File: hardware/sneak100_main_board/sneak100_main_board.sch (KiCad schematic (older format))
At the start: 0 parts

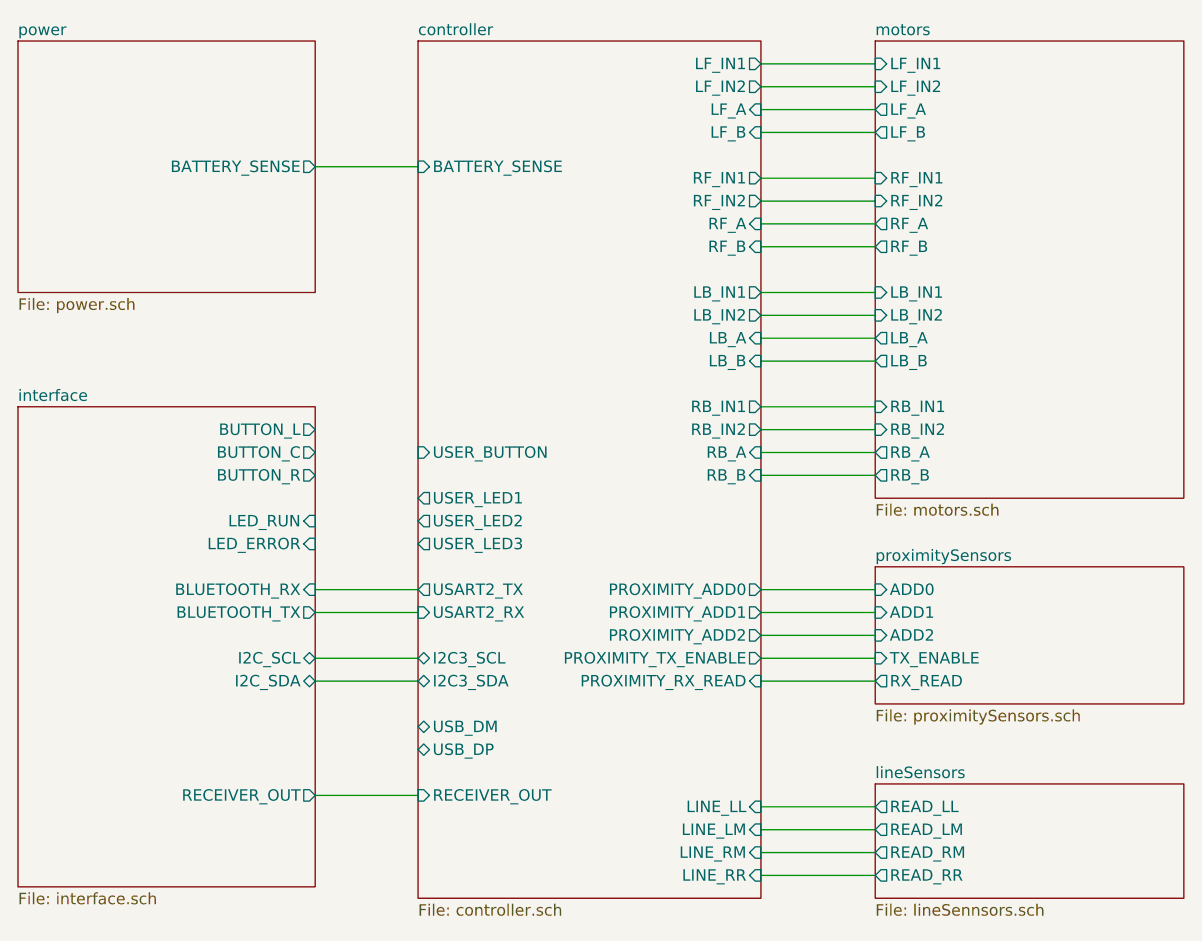
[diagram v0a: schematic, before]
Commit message: Board interface layout
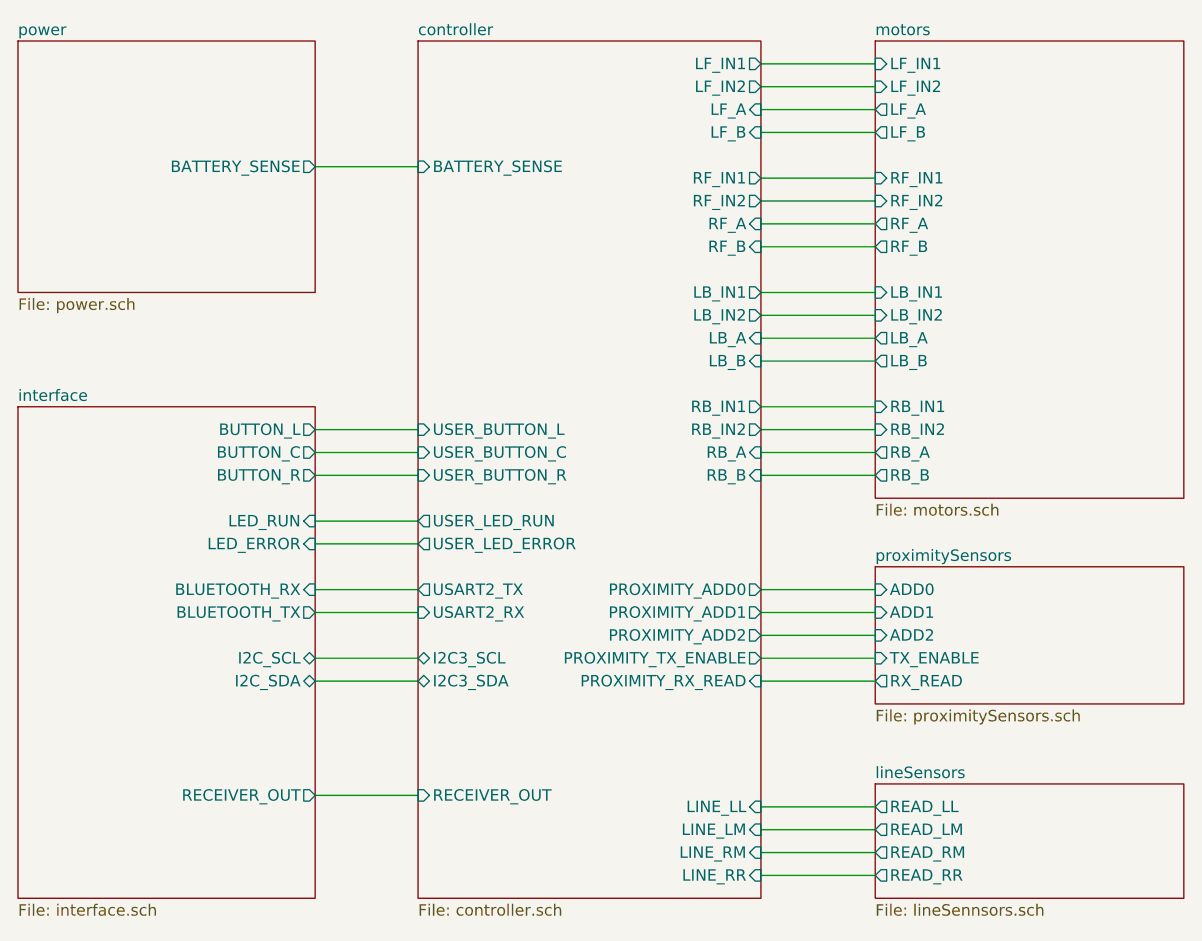
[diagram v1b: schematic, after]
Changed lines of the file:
@@
 F7 "LB_B" I R 6400 3300 50
 F8 "I2C3_SCL" B L 4900 4600 50
-F9 "USB_DM" B L 4900 4900 50
-F10 "USB_DP" B L 4900 5000 50
-F11 "USER_LED1" O L 4900 3900 50
-F12 "LB_IN1" O R 6400 3000 50
-F13 "LB_IN2" O R 6400 3100 50
-F14 "PROXIMITY_ADD0" O R 6400 4300 50
-F15 "PROXIMITY_ADD1" O R 6400 4400 50
-F16 "PROXIMITY_ADD2" O R 6400 4500 50
-F17 "RB_A" I R 6400 3700 50
-F18 "RB_B" I R 6400 3800 50
-F19 "RB_IN1" O R 6400 3500 50
-F20 "RB_IN2" O R 6400 3600 50
-F21 "RF_IN1" O R 6400 2500 50
-F22 "RF_IN2" O R 6400 2600 50
-F23 "LF_IN1" O R 6400 2000 50
-F24 "LF_IN2" O R 6400 2100 50
-F25 "LINE_LL" I R 6400 5250 50
-F26 "LINE_LM" I R 6400 5350 50
-F27 "LINE_RM" I R 6400 5450 50
-F28 "LINE_RR" I R 6400 5550 50
-F29 "BATTERY_SENSE" I L 4900 2450 50
-F30 "PROXIMITY_RX_READ" I R 6400 4700 50
-F31 "LF_A" I R 6400 2200 50
-F32 "LF_B" I R 6400 2300 50
-F33 "PROXIMITY_TX_ENABLE" O R 6400 4600 50
-F34 "I2C3_SDA" B L 4900 4700 50
-F35 "USER_LED2" O L 4900 4000 50
-F36 "USER_LED3" O L 4900 4100 50
-F37 "USER_BUTTON" I L 4900 3700 50
-F38 "RECEIVER_OUT" I L 4900 5200 50
+F9 "LB_IN1" O R 6400 3000 50
+F10 "LB_IN2" O R 6400 3100 50
+F11 "PROXIMITY_ADD0" O R 6400 4300 50
+F12 "PROXIMITY_ADD1" O R 6400 4400 50
+F13 "PROXIMITY_ADD2" O R 6400 4500 50
+F14 "RB_A" I R 6400 3700 50
+F15 "RB_B" I R 6400 3800 50
+F16 "RB_IN1" O R 6400 3500 50
+F17 "RB_IN2" O R 6400 3600 50
+F18 "RF_IN1" O R 6400 2500 50
+F19 "RF_IN2" O R 6400 2600 50
+F20 "LF_IN1" O R 6400 2000 50
+F21 "LF_IN2" O R 6400 2100 50
+F22 "LINE_LL" I R 6400 5250 50
+F23 "LINE_LM" I R 6400 5350 50
+F24 "LINE_RM" I R 6400 5450 50
+F25 "LINE_RR" I R 6400 5550 50
+F26 "BATTERY_SENSE" I L 4900 2450 50
+F27 "PROXIMITY_RX_READ" I R 6400 4700 50
+F28 "LF_A" I R 6400 2200 50
+F29 "LF_B" I R 6400 2300 50
+F30 "PROXIMITY_TX_ENABLE" O R 6400 4600 50
+F31 "I2C3_SDA" B L 4900 4700 50
+F32 "RECEIVER_OUT" I L 4900 5200 50
+F33 "USER_LED_RUN" O L 4900 4000 50
+F34 "USER_LED_ERROR" O L 4900 4100 50
+F35 "USER_BUTTON_C" I L 4900 3700 50
+F36 "USER_BUTTON_L" I L 4900 3600 50
+F37 "USER_BUTTON_R" I L 4900 3800 50
 $EndSheet
 $Sheet
-S 3150 3500 1300 2100
+S 3150 3500 1300 2150
 U 60E0491A
 F0 "interface" 50
@@
 F11 "LED_ERROR" I R 4450 4100 50
 $EndSheet
+Wire Wire Line
+	4450 3600 4900 3600
+Wire Wire Line
+	4450 3700 4900 3700
+Wire Wire Line
+	4450 3800 4900 3800
+Wire Wire Line
+	4450 4000 4900 4000
+Wire Wire Line
+	4450 4100 4900 4100
 $EndSCHEMATC

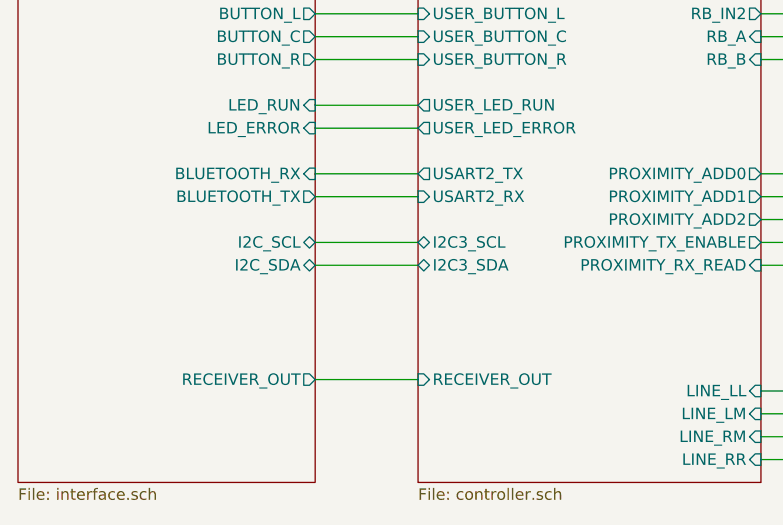
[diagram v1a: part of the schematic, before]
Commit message: bluetooth en & status connection
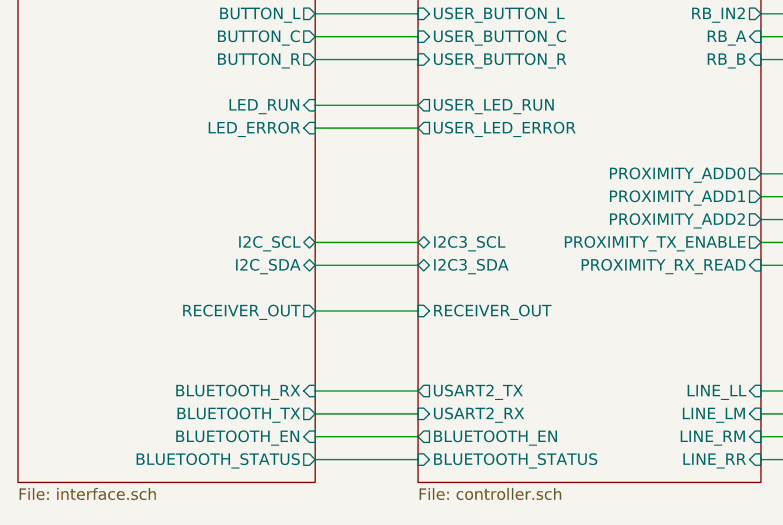
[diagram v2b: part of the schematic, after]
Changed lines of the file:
@@
 	6400 5550 6900 5550
 Wire Wire Line
-	4900 4300 4450 4300
+	4900 5250 4450 5250
 Wire Wire Line
-	4900 4400 4450 4400
+	4900 5350 4450 5350
 Wire Wire Line
 	4900 4600 4450 4600
@@
 	4900 4700 4450 4700
 Wire Wire Line
-	4450 5200 4900 5200
+	4450 4900 4900 4900
 Wire Wire Line
 	4450 2450 4900 2450
@@
 F2 "RF_A" I R 6400 2700 50
 F3 "RF_B" I R 6400 2800 50
-F4 "USART2_TX" O L 4900 4300 50
-F5 "USART2_RX" I L 4900 4400 50
+F4 "USART2_TX" O L 4900 5250 50
+F5 "USART2_RX" I L 4900 5350 50
 F6 "LB_A" I R 6400 3200 50
 F7 "LB_B" I R 6400 3300 50
@@
 F30 "PROXIMITY_TX_ENABLE" O R 6400 4600 50
 F31 "I2C3_SDA" B L 4900 4700 50
-F32 "RECEIVER_OUT" I L 4900 5200 50
+F32 "RECEIVER_OUT" I L 4900 4900 50
 F33 "USER_LED_RUN" O L 4900 4000 50
 F34 "USER_LED_ERROR" O L 4900 4100 50
@@
 F36 "USER_BUTTON_L" I L 4900 3600 50
 F37 "USER_BUTTON_R" I L 4900 3800 50
+F38 "BLUETOOTH_EN" O L 4900 5450 50
+F39 "BLUETOOTH_STATUS" I L 4900 5550 50
 $EndSheet
 $Sheet
@@
 F0 "interface" 50
 F1 "interface.sch" 50
-F2 "BLUETOOTH_RX" I R 4450 4300 50
-F3 "BLUETOOTH_TX" O R 4450 4400 50
+F2 "BLUETOOTH_RX" I R 4450 5250 50
+F3 "BLUETOOTH_TX" O R 4450 5350 50
 F4 "I2C_SDA" B R 4450 4700 50
 F5 "I2C_SCL" B R 4450 4600 50
-F6 "RECEIVER_OUT" O R 4450 5200 50
+F6 "RECEIVER_OUT" O R 4450 4900 50
 F7 "BUTTON_L" O R 4450 3600 50
 F8 "LED_RUN" I R 4450 4000 50
@@
 F10 "BUTTON_R" O R 4450 3800 50
 F11 "LED_ERROR" I R 4450 4100 50
+F12 "BLUETOOTH_EN" I R 4450 5450 50
+F13 "BLUETOOTH_STATUS" O R 4450 5550 50
 $EndSheet
 Wire Wire Line
@@
 Wire Wire Line
 	4450 4100 4900 4100
+Wire Wire Line
+	4900 5450 4450 5450
+Wire Wire Line
+	4900 5550 4450 5550
 $EndSCHEMATC

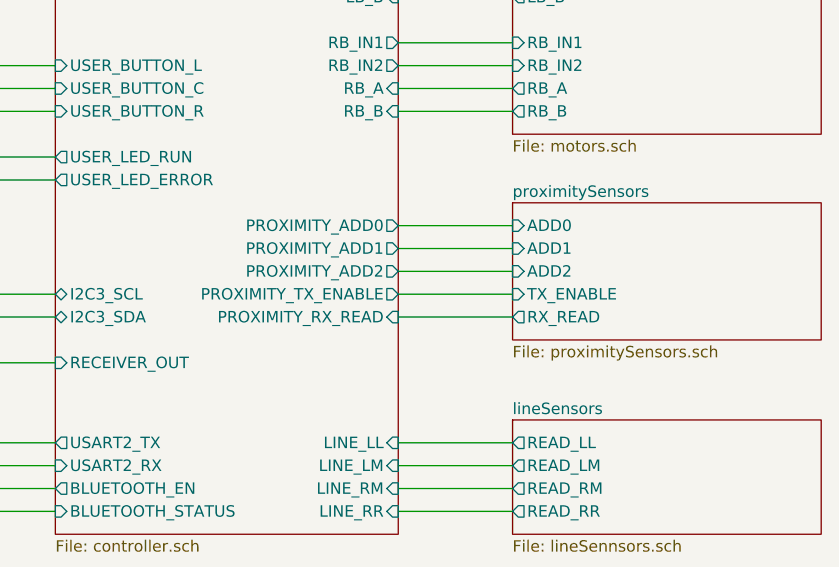
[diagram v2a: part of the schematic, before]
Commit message: Add external proximity sensor, erase old from schematic
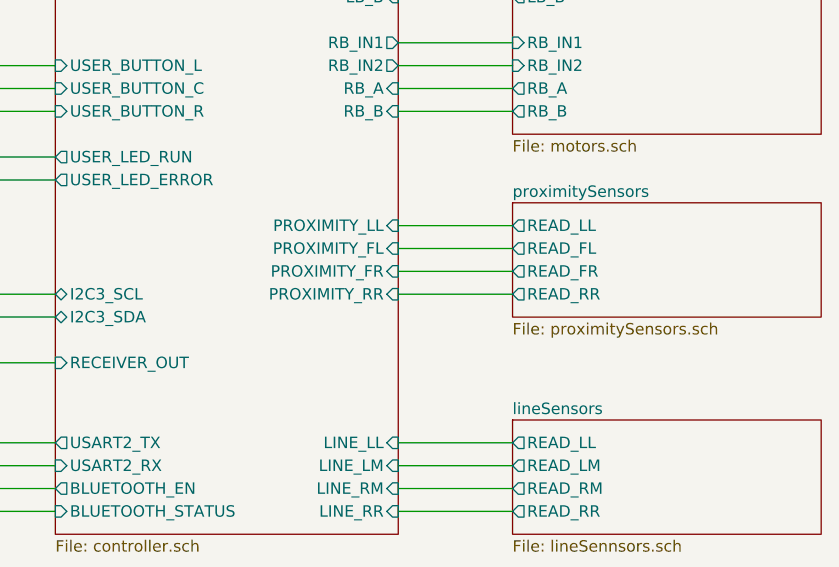
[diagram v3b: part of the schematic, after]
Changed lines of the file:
@@
-$EndSheet
-$Sheet
-S 6900 4200 1350 600
-U 60E049FE
-F0 "proximitySensors" 50
-F1 "proximitySensors.sch" 50
-F2 "RX_READ" O L 6900 4700 50
-F3 "TX_ENABLE" I L 6900 4600 50
-F4 "ADD0" I L 6900 4300 50
-F5 "ADD1" I L 6900 4400 50
-F6 "ADD2" I L 6900 4500 50
 $EndSheet
 $Sheet
@@
 	6400 4600 6900 4600
 Wire Wire Line
-	6400 4700 6900 4700
-Wire Wire Line
 	6400 5250 6900 5250
 Wire Wire Line
@@
 Wire Wire Line
 	4450 2450 4900 2450
-$Sheet
-S 4900 1900 1500 3750
-U 6100FE40
-F0 "controller" 50
-F1 "controller.sch" 50
-F2 "RF_A" I R 6400 2700 50
-F3 "RF_B" I R 6400 2800 50
-F4 "USART2_TX" O L 4900 5250 50
-F5 "USART2_RX" I L 4900 5350 50
-F6 "LB_A" I R 6400 3200 50
-F7 "LB_B" I R 6400 3300 50
-F8 "I2C3_SCL" B L 4900 4600 50
-F9 "LB_IN1" O R 6400 3000 50
-F10 "LB_IN2" O R 6400 3100 50
-F11 "PROXIMITY_ADD0" O R 6400 4300 50
-F12 "PROXIMITY_ADD1" O R 6400 4400 50
-F13 "PROXIMITY_ADD2" O R 6400 4500 50
-F14 "RB_A" I R 6400 3700 50
-F15 "RB_B" I R 6400 3800 50
-F16 "RB_IN1" O R 6400 3500 50
-F17 "RB_IN2" O R 6400 3600 50
-F18 "RF_IN1" O R 6400 2500 50
-F19 "RF_IN2" O R 6400 2600 50
-F20 "LF_IN1" O R 6400 2000 50
-F21 "LF_IN2" O R 6400 2100 50
-F22 "LINE_LL" I R 6400 5250 50
-F23 "LINE_LM" I R 6400 5350 50
-F24 "LINE_RM" I R 6400 5450 50
-F25 "LINE_RR" I R 6400 5550 50
-F26 "BATTERY_SENSE" I L 4900 2450 50
-F27 "PROXIMITY_RX_READ" I R 6400 4700 50
-F28 "LF_A" I R 6400 2200 50
-F29 "LF_B" I R 6400 2300 50
-F30 "PROXIMITY_TX_ENABLE" O R 6400 4600 50
-F31 "I2C3_SDA" B L 4900 4700 50
-F32 "RECEIVER_OUT" I L 4900 4900 50
-F33 "USER_LED_RUN" O L 4900 4000 50
-F34 "USER_LED_ERROR" O L 4900 4100 50
-F35 "USER_BUTTON_C" I L 4900 3700 50
-F36 "USER_BUTTON_L" I L 4900 3600 50
-F37 "USER_BUTTON_R" I L 4900 3800 50
-F38 "BLUETOOTH_EN" O L 4900 5450 50
-F39 "BLUETOOTH_STATUS" I L 4900 5550 50
-$EndSheet
 $Sheet
 S 3150 3500 1300 2150
@@
 Wire Wire Line
 	4900 5550 4450 5550
+$Sheet
+S 6900 4200 1350 500
+U 60E049FE
+F0 "proximitySensors" 50
+F1 "proximitySensors.sch" 50
+F2 "READ_LL" O L 6900 4300 50
+F3 "READ_FL" O L 6900 4400 50
+F4 "READ_FR" O L 6900 4500 50
+F5 "READ_RR" O L 6900 4600 50
+$EndSheet
+$Sheet
+S 4900 1900 1500 3750
+U 6100FE40
+F0 "controller" 50
+F1 "controller.sch" 50
+F2 "RF_A" I R 6400 2700 50
+F3 "RF_B" I R 6400 2800 50
+F4 "USART2_TX" O L 4900 5250 50
+F5 "USART2_RX" I L 4900 5350 50
+F6 "LB_A" I R 6400 3200 50
+F7 "LB_B" I R 6400 3300 50
+F8 "I2C3_SCL" B L 4900 4600 50
+F9 "LB_IN1" O R 6400 3000 50
+F10 "LB_IN2" O R 6400 3100 50
+F11 "RB_A" I R 6400 3700 50
+F12 "RB_B" I R 6400 3800 50
+F13 "RB_IN1" O R 6400 3500 50
+F14 "RB_IN2" O R 6400 3600 50
+F15 "RF_IN1" O R 6400 2500 50
+F16 "RF_IN2" O R 6400 2600 50
+F17 "LF_IN1" O R 6400 2000 50
+F18 "LF_IN2" O R 6400 2100 50
+F19 "LINE_LL" I R 6400 5250 50
+F20 "LINE_LM" I R 6400 5350 50
+F21 "LINE_RM" I R 6400 5450 50
+F22 "LINE_RR" I R 6400 5550 50
+F23 "BATTERY_SENSE" I L 4900 2450 50
+F24 "LF_A" I R 6400 2200 50
+F25 "LF_B" I R 6400 2300 50
+F26 "I2C3_SDA" B L 4900 4700 50
+F27 "RECEIVER_OUT" I L 4900 4900 50
+F28 "USER_LED_RUN" O L 4900 4000 50
+F29 "USER_LED_ERROR" O L 4900 4100 50
+F30 "USER_BUTTON_C" I L 4900 3700 50
+F31 "USER_BUTTON_L" I L 4900 3600 50
+F32 "USER_BUTTON_R" I L 4900 3800 50
+F33 "BLUETOOTH_EN" O L 4900 5450 50
+F34 "BLUETOOTH_STATUS" I L 4900 5550 50
+F35 "PROXIMITY_LL" I R 6400 4300 50
+F36 "PROXIMITY_FL" I R 6400 4400 50
+F37 "PROXIMITY_FR" I R 6400 4500 50
+F38 "PROXIMITY_RR" I R 6400 4600 50
+$EndSheet
 $EndSCHEMATC
